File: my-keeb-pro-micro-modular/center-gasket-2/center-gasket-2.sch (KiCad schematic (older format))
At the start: 50 parts, among them M1 1x5, M2 1x5, SW1 SW_Push, U1 ProMicro

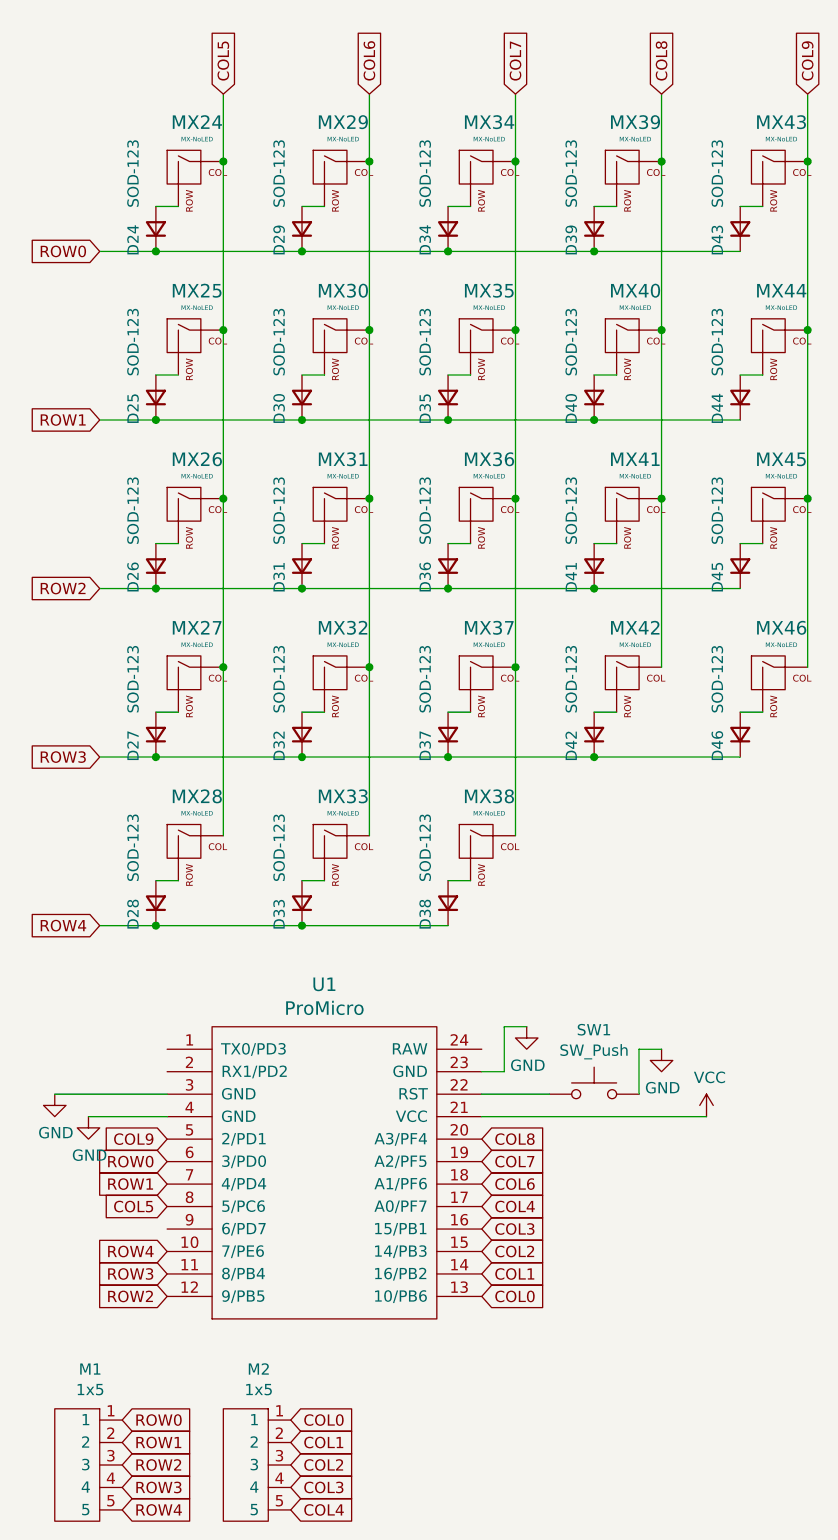
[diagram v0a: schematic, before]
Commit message: Added a gasket mount case file
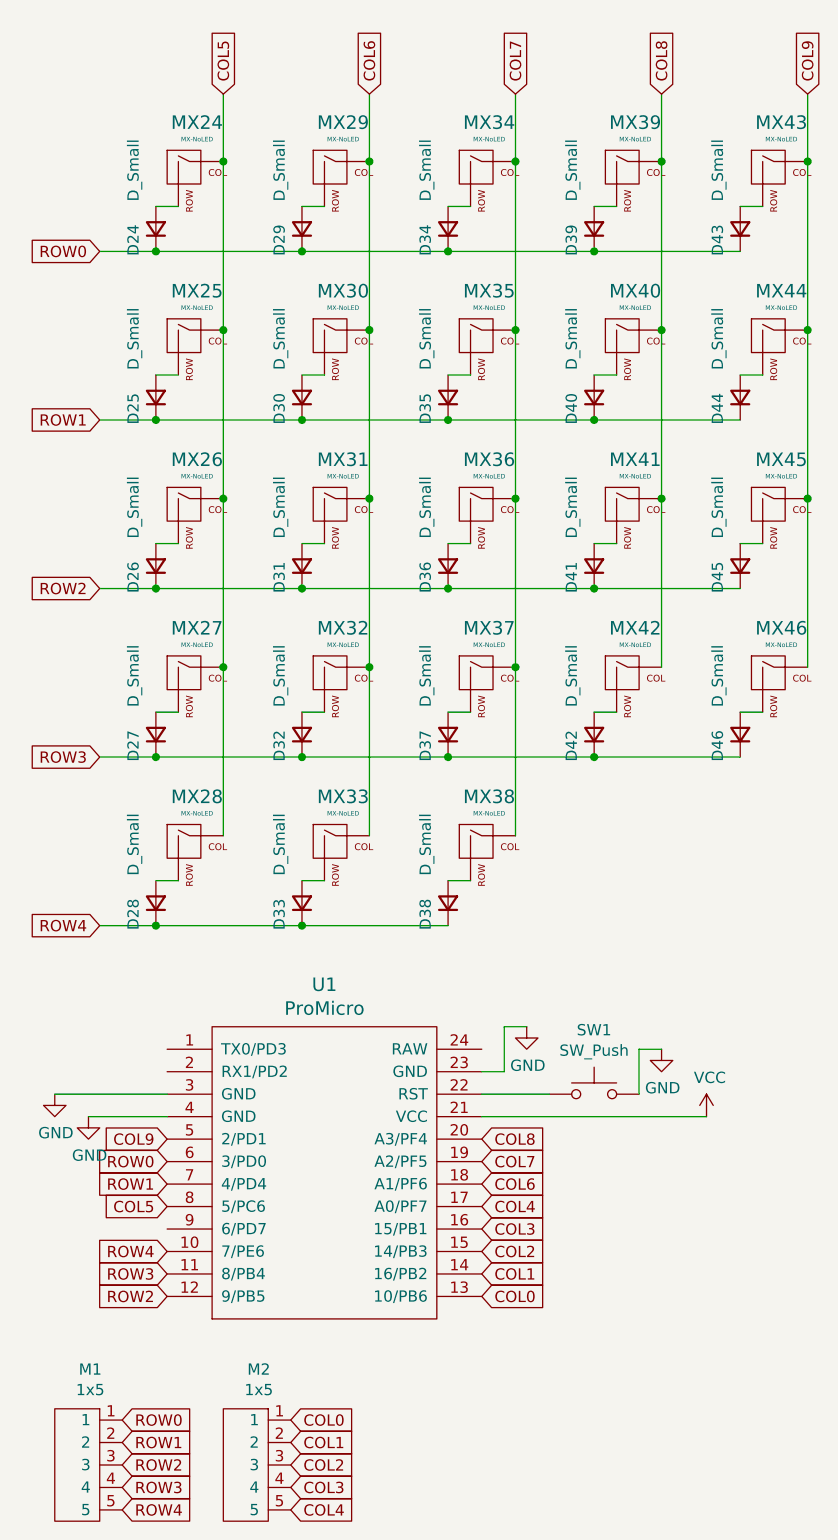
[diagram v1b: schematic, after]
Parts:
- D24, D25, D26, D27, D28, D29, D30, D31, D32, D33, D34, D35, D36, D37, D38, D39, D40, D41, D42, D43, D44, D45, D46: value SOD-123 -> D_Small
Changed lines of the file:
@@
 P 2450 4500
 F 0 "D38" H 2400 4600 50  0000 C CNN
-F 1 "SOD-123" H 2850 4600 50  0000 R CNN
+F 1 "D_Small" H 2850 4600 50  0000 R CNN
 F 2 "Keebio-Parts:Diode-Hybrid-Back" V 2450 4500 50  0001 C CNN
 F 3 "~" V 2450 4500 50  0001 C CNN
@@
 P 1150 4500
 F 0 "D28" H 1100 4600 50  0000 C CNN
-F 1 "SOD-123" H 1550 4600 50  0000 R CNN
+F 1 "D_Small" H 1550 4600 50  0000 R CNN
 F 2 "Keebio-Parts:Diode-Hybrid-Back" V 1150 4500 50  0001 C CNN
 F 3 "~" V 1150 4500 50  0001 C CNN
@@
 P 1800 4500
 F 0 "D33" H 1750 4600 50  0000 C CNN
-F 1 "SOD-123" H 2200 4600 50  0000 R CNN
+F 1 "D_Small" H 2200 4600 50  0000 R CNN
 F 2 "Keebio-Parts:Diode-Hybrid-Back" V 1800 4500 50  0001 C CNN
 F 3 "~" V 1800 4500 50  0001 C CNN
@@
 P 1150 2250
 F 0 "D25" H 1100 2350 50  0000 C CNN
-F 1 "SOD-123" H 1550 2350 50  0000 R CNN
+F 1 "D_Small" H 1550 2350 50  0000 R CNN
 F 2 "Keebio-Parts:Diode-Hybrid-Back" V 1150 2250 50  0001 C CNN
 F 3 "~" V 1150 2250 50  0001 C CNN
@@
 P 1800 2250
 F 0 "D30" H 1750 2350 50  0000 C CNN
-F 1 "SOD-123" H 2200 2350 50  0000 R CNN
+F 1 "D_Small" H 2200 2350 50  0000 R CNN
 F 2 "Keebio-Parts:Diode-Hybrid-Back" V 1800 2250 50  0001 C CNN
 F 3 "~" V 1800 2250 50  0001 C CNN
@@
 P 2450 2250
 F 0 "D35" H 2400 2350 50  0000 C CNN
-F 1 "SOD-123" H 2850 2350 50  0000 R CNN
+F 1 "D_Small" H 2850 2350 50  0000 R CNN
 F 2 "Keebio-Parts:Diode-Hybrid-Back" V 2450 2250 50  0001 C CNN
 F 3 "~" V 2450 2250 50  0001 C CNN
@@
 P 3100 2250
 F 0 "D40" H 3050 2350 50  0000 C CNN
-F 1 "SOD-123" H 3500 2350 50  0000 R CNN
+F 1 "D_Small" H 3500 2350 50  0000 R CNN
 F 2 "Keebio-Parts:Diode-Hybrid-Back" V 3100 2250 50  0001 C CNN
 F 3 "~" V 3100 2250 50  0001 C CNN
@@
 P 3750 2250
 F 0 "D44" H 3700 2350 50  0000 C CNN
-F 1 "SOD-123" H 4150 2350 50  0000 R CNN
+F 1 "D_Small" H 4150 2350 50  0000 R CNN
 F 2 "Keebio-Parts:Diode-Hybrid-Back" V 3750 2250 50  0001 C CNN
 F 3 "~" V 3750 2250 50  0001 C CNN
@@
 P 1150 3000
 F 0 "D26" H 1100 3100 50  0000 C CNN
-F 1 "SOD-123" H 1550 3100 50  0000 R CNN
+F 1 "D_Small" H 1550 3100 50  0000 R CNN
 F 2 "Keebio-Parts:Diode-Hybrid-Back" V 1150 3000 50  0001 C CNN
 F 3 "~" V 1150 3000 50  0001 C CNN
@@
 P 1800 3000
 F 0 "D31" H 1750 3100 50  0000 C CNN
-F 1 "SOD-123" H 2200 3100 50  0000 R CNN
+F 1 "D_Small" H 2200 3100 50  0000 R CNN
 F 2 "Keebio-Parts:Diode-Hybrid-Back" V 1800 3000 50  0001 C CNN
 F 3 "~" V 1800 3000 50  0001 C CNN
@@
 P 2450 3000
 F 0 "D36" H 2400 3100 50  0000 C CNN
-F 1 "SOD-123" H 2850 3100 50  0000 R CNN
+F 1 "D_Small" H 2850 3100 50  0000 R CNN
 F 2 "Keebio-Parts:Diode-Hybrid-Back" V 2450 3000 50  0001 C CNN
 F 3 "~" V 2450 3000 50  0001 C CNN
@@
 P 3100 3000
 F 0 "D41" H 3050 3100 50  0000 C CNN
-F 1 "SOD-123" H 3500 3100 50  0000 R CNN
+F 1 "D_Small" H 3500 3100 50  0000 R CNN
 F 2 "Keebio-Parts:Diode-Hybrid-Back" V 3100 3000 50  0001 C CNN
 F 3 "~" V 3100 3000 50  0001 C CNN
@@
 P 3750 3000
 F 0 "D45" H 3700 3100 50  0000 C CNN
-F 1 "SOD-123" H 4150 3100 50  0000 R CNN
+F 1 "D_Small" H 4150 3100 50  0000 R CNN
 F 2 "Keebio-Parts:Diode-Hybrid-Back" V 3750 3000 50  0001 C CNN
 F 3 "~" V 3750 3000 50  0001 C CNN
@@
 P 1150 3750
 F 0 "D27" H 1100 3850 50  0000 C CNN
-F 1 "SOD-123" H 1550 3850 50  0000 R CNN
+F 1 "D_Small" H 1550 3850 50  0000 R CNN
 F 2 "Keebio-Parts:Diode-Hybrid-Back" V 1150 3750 50  0001 C CNN
 F 3 "~" V 1150 3750 50  0001 C CNN
@@
 P 1800 3750
 F 0 "D32" H 1750 3850 50  0000 C CNN
-F 1 "SOD-123" H 2200 3850 50  0000 R CNN
+F 1 "D_Small" H 2200 3850 50  0000 R CNN
 F 2 "Keebio-Parts:Diode-Hybrid-Back" V 1800 3750 50  0001 C CNN
 F 3 "~" V 1800 3750 50  0001 C CNN
@@
 P 2450 3750
 F 0 "D37" H 2400 3850 50  0000 C CNN
-F 1 "SOD-123" H 2850 3850 50  0000 R CNN
+F 1 "D_Small" H 2850 3850 50  0000 R CNN
 F 2 "Keebio-Parts:Diode-Hybrid-Back" V 2450 3750 50  0001 C CNN
 F 3 "~" V 2450 3750 50  0001 C CNN
@@
 P 3100 3750
 F 0 "D42" H 3050 3850 50  0000 C CNN
-F 1 "SOD-123" H 3500 3850 50  0000 R CNN
+F 1 "D_Small" H 3500 3850 50  0000 R CNN
 F 2 "Keebio-Parts:Diode-Hybrid-Back" V 3100 3750 50  0001 C CNN
 F 3 "~" V 3100 3750 50  0001 C CNN
@@
 P 3750 3750
 F 0 "D46" H 3700 3850 50  0000 C CNN
-F 1 "SOD-123" H 4150 3850 50  0000 R CNN
+F 1 "D_Small" H 4150 3850 50  0000 R CNN
 F 2 "Keebio-Parts:Diode-Hybrid-Back" V 3750 3750 50  0001 C CNN
 F 3 "~" V 3750 3750 50  0001 C CNN
@@
 P 3750 1500
 F 0 "D43" H 3700 1600 50  0000 C CNN
-F 1 "SOD-123" H 4150 1600 50  0000 R CNN
+F 1 "D_Small" H 4150 1600 50  0000 R CNN
 F 2 "Keebio-Parts:Diode-Hybrid-Back" V 3750 1500 50  0001 C CNN
 F 3 "~" V 3750 1500 50  0001 C CNN
@@
 P 3100 1500
 F 0 "D39" H 3050 1600 50  0000 C CNN
-F 1 "SOD-123" H 3500 1600 50  0000 R CNN
+F 1 "D_Small" H 3500 1600 50  0000 R CNN
 F 2 "Keebio-Parts:Diode-Hybrid-Back" V 3100 1500 50  0001 C CNN
 F 3 "~" V 3100 1500 50  0001 C CNN
@@
 P 2450 1500
 F 0 "D34" H 2400 1600 50  0000 C CNN
-F 1 "SOD-123" H 2850 1600 50  0000 R CNN
+F 1 "D_Small" H 2850 1600 50  0000 R CNN
 F 2 "Keebio-Parts:Diode-Hybrid-Back" V 2450 1500 50  0001 C CNN
 F 3 "~" V 2450 1500 50  0001 C CNN
@@
 P 1800 1500
 F 0 "D29" H 1750 1600 50  0000 C CNN
-F 1 "SOD-123" H 2200 1600 50  0000 R CNN
+F 1 "D_Small" H 2200 1600 50  0000 R CNN
 F 2 "Keebio-Parts:Diode-Hybrid-Back" V 1800 1500 50  0001 C CNN
 F 3 "~" V 1800 1500 50  0001 C CNN
@@
 P 1150 1500
 F 0 "D24" H 1100 1600 50  0000 C CNN
-F 1 "SOD-123" H 1550 1600 50  0000 R CNN
+F 1 "D_Small" H 1550 1600 50  0000 R CNN
 F 2 "Keebio-Parts:Diode-Hybrid-Back" V 1150 1500 50  0001 C CNN
 F 3 "~" V 1150 1500 50  0001 C CNN
